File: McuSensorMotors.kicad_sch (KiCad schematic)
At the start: 1 part, among them U1 NUCLEO-G474RE

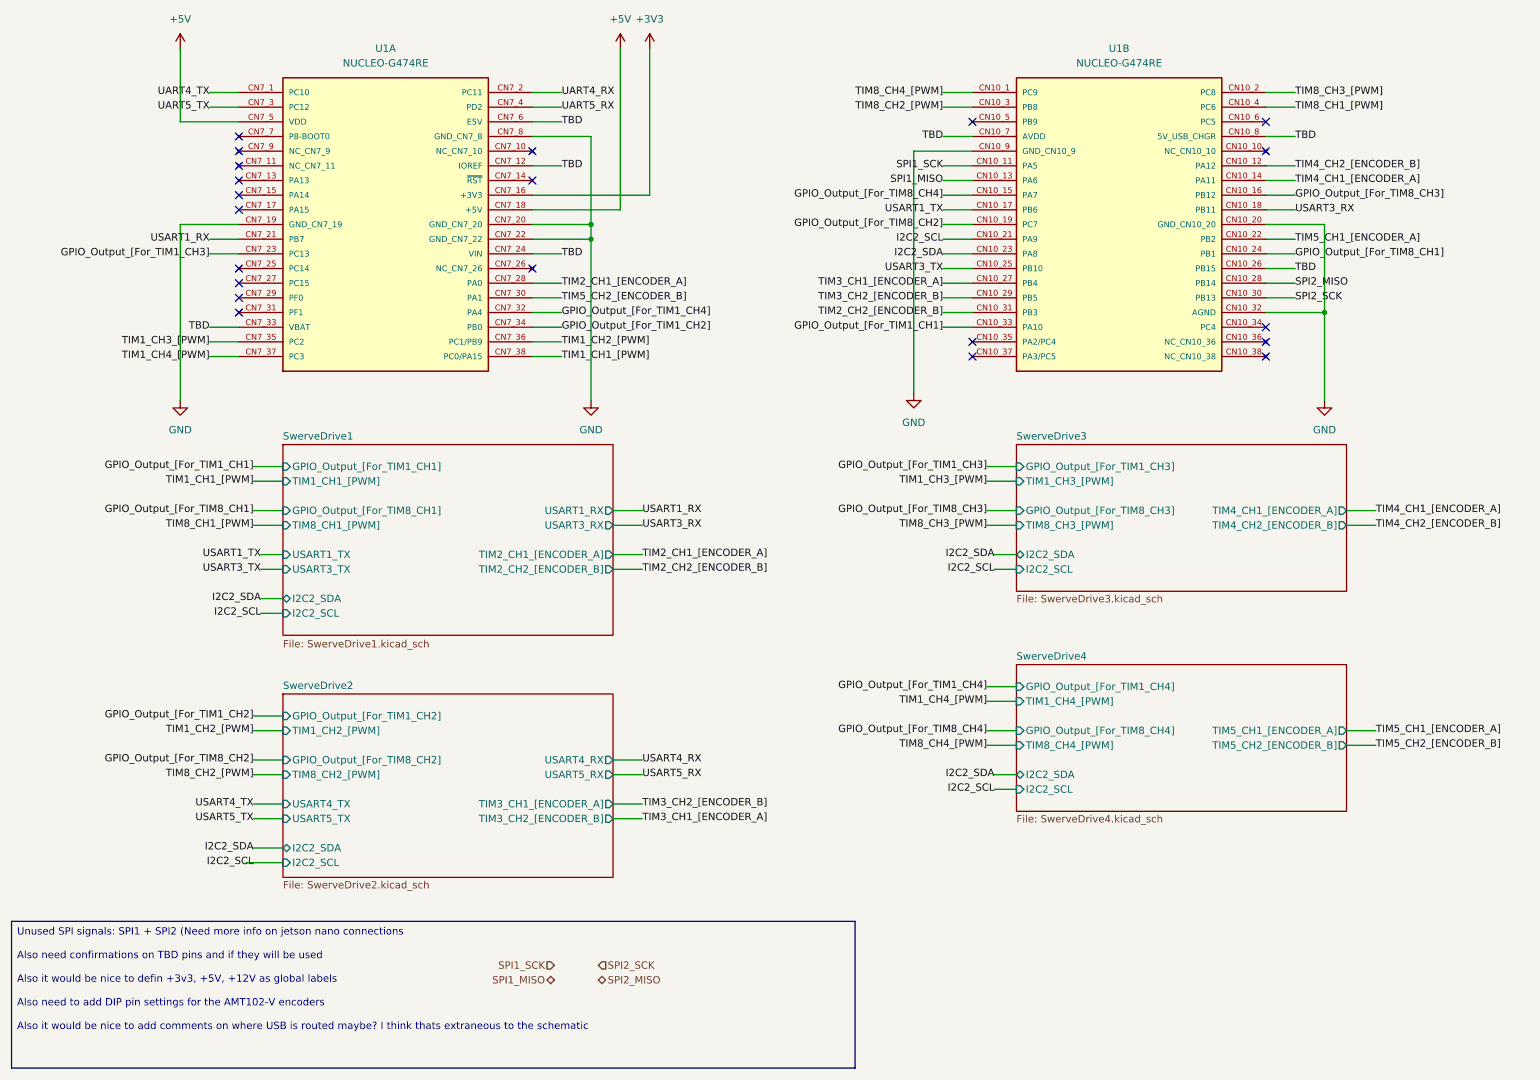
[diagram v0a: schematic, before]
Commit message: Added loop testing GPIO + removed SPI1 + moved TIM2/TIM5 to nicer pins
_
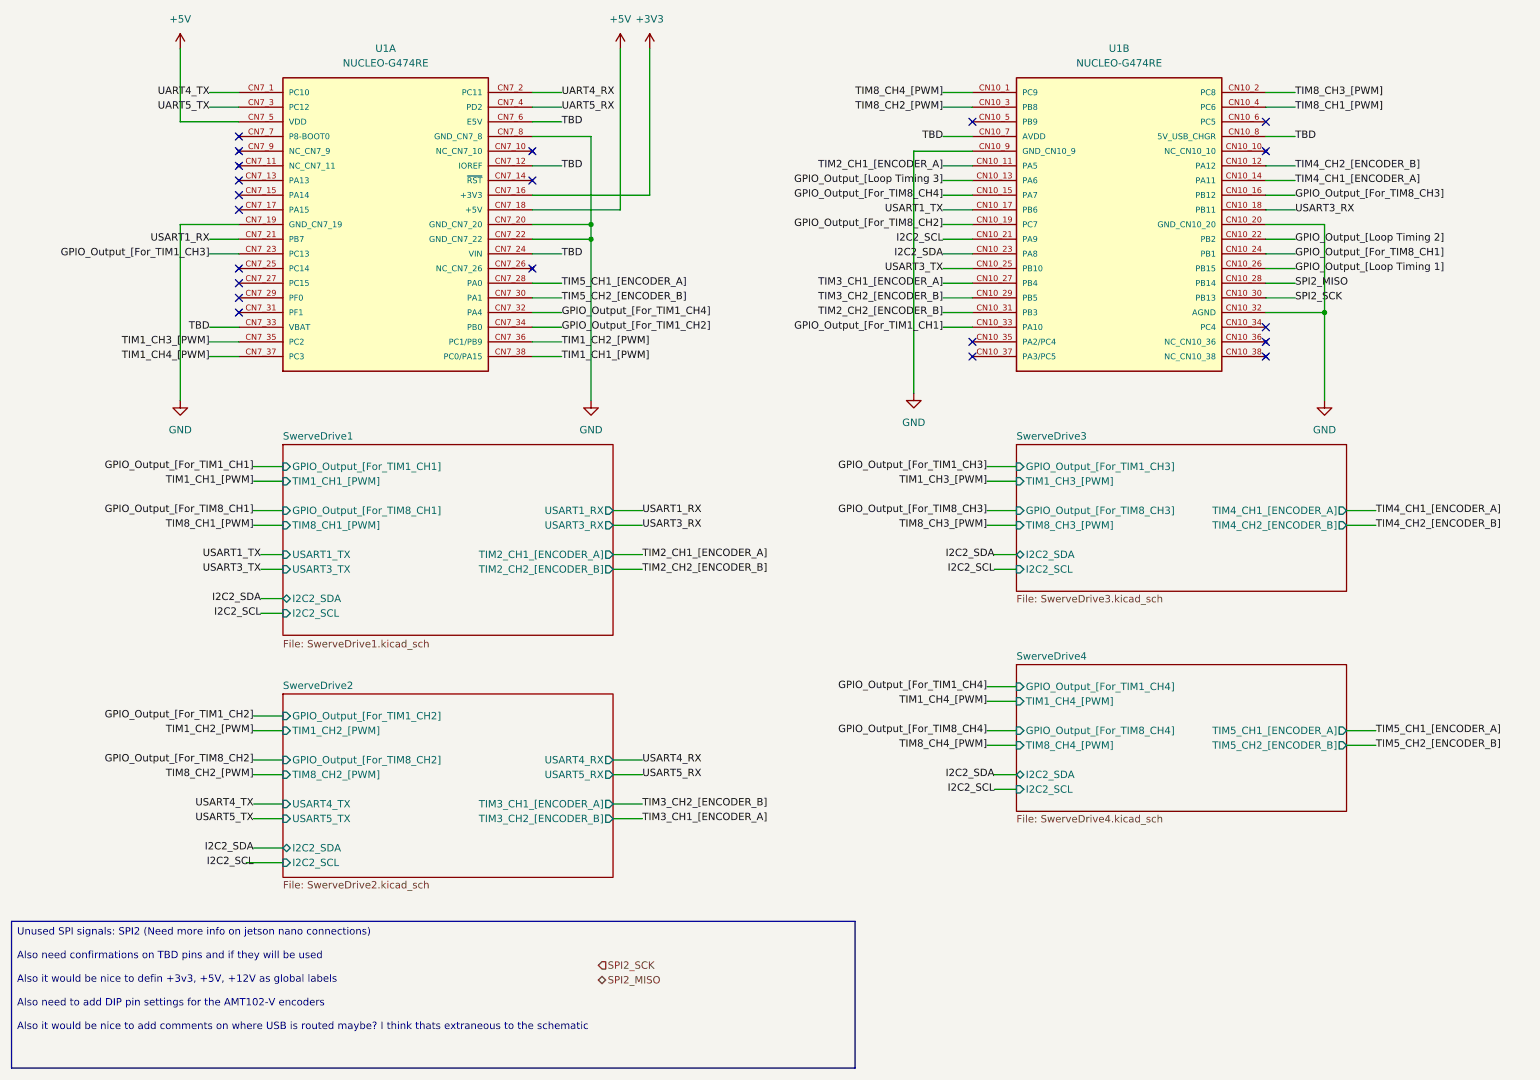
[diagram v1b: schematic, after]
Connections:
- net SPI1_SCK is gone; now on net TIM2_CH1_[ENCODER_A]: U1.CN10_11 (PA5)
- net TBD: no longer U1.CN10_26 (PB15)
- net TIM2_CH1_[ENCODER_A]: no longer U1.CN7_28 (PA0)
- net TIM5_CH1_[ENCODER_A]: now also U1.CN7_28 (PA0); no longer U1.CN10_22 (PB2)
- net SPI1_MISO renamed GPIO_Output_[Loop Timing 3]
- new net GPIO_Output_[Loop Timing 1]: U1.CN10_26 (PB15)
- new net GPIO_Output_[Loop Timing 2]: U1.CN10_22 (PB2)
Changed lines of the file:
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@@
 		)
 	)
-	(text_box "Unused SPI signals: SPI1 + SPI2 (Need more info on jetson nano connections\n\nAlso need confirmations on TBD pins and if they will be used\n\nAlso it would be nice to defin +3v3, +5V, +12V as global labels\n\nAlso need to add DIP pin settings for the AMT102-V encoders\n\nAlso it would be nice to add comments on where USB is routed maybe? I think thats extraneous to the schematic\n"
+	(text_box "Unused SPI signals: SPI2 (Need more info on jetson nano connections)\n\nAlso need confirmations on TBD pins and if they will be used\n\nAlso it would be nice to defin +3v3, +5V, +12V as global labels\n\nAlso need to add DIP pin settings for the AMT102-V encoders\n\nAlso it would be nice to add comments on where USB is routed maybe? I think thats extraneous to the schematic\n"
 		(exclude_from_sim no)
 		(at 16.51 171.45 0)
@@
 		)
 	)
-	(label "TBD"
+	(label "GPIO_Output_[Loop Timing 1]"
 		(at 238.76 58.42 0)
 		(effects
@@
 		)
 	)
-	(label "SPI1_SCK"
+	(label "TIM2_CH1_[ENCODER_A]"
 		(at 177.8 40.64 180)
 		(effects
@@
 		)
 	)
-	(label "TIM2_CH1_[ENCODER_A]"
+	(label "TIM5_CH1_[ENCODER_A]"
 		(at 111.76 60.96 0)
 		(effects
@@
 		)
 	)
-	(label "TIM5_CH1_[ENCODER_A]"
+	(label "GPIO_Output_[Loop Timing 2]"
 		(at 238.76 53.34 0)
 		(effects
@@
 		)
 	)
-	(label "SPI1_MISO"
+	(label "GPIO_Output_[Loop Timing 3]"
 		(at 177.8 43.18 180)
 		(effects
@@
 		)
 	)
-	(hierarchical_label "SPI1_MISO"
-		(shape bidirectional)
-		(at 110.49 181.61 180)
-		(effects
-			(font
-				(size 1.27 1.27)
-			)
-			(justify right)
-		)
-	)
-	(hierarchical_label "SPI1_SCK"
-		(shape input)
-		(at 110.49 179.07 180)
-		(effects
-			(font
-				(size 1.27 1.27)
-			)
-			(justify right)
-		)
-	)
